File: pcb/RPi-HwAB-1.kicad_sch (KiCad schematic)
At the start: 8 parts, among them J1 GPIO, J2 Hirose_FH12-16S, J3 TC2050, U1 CAT24C256

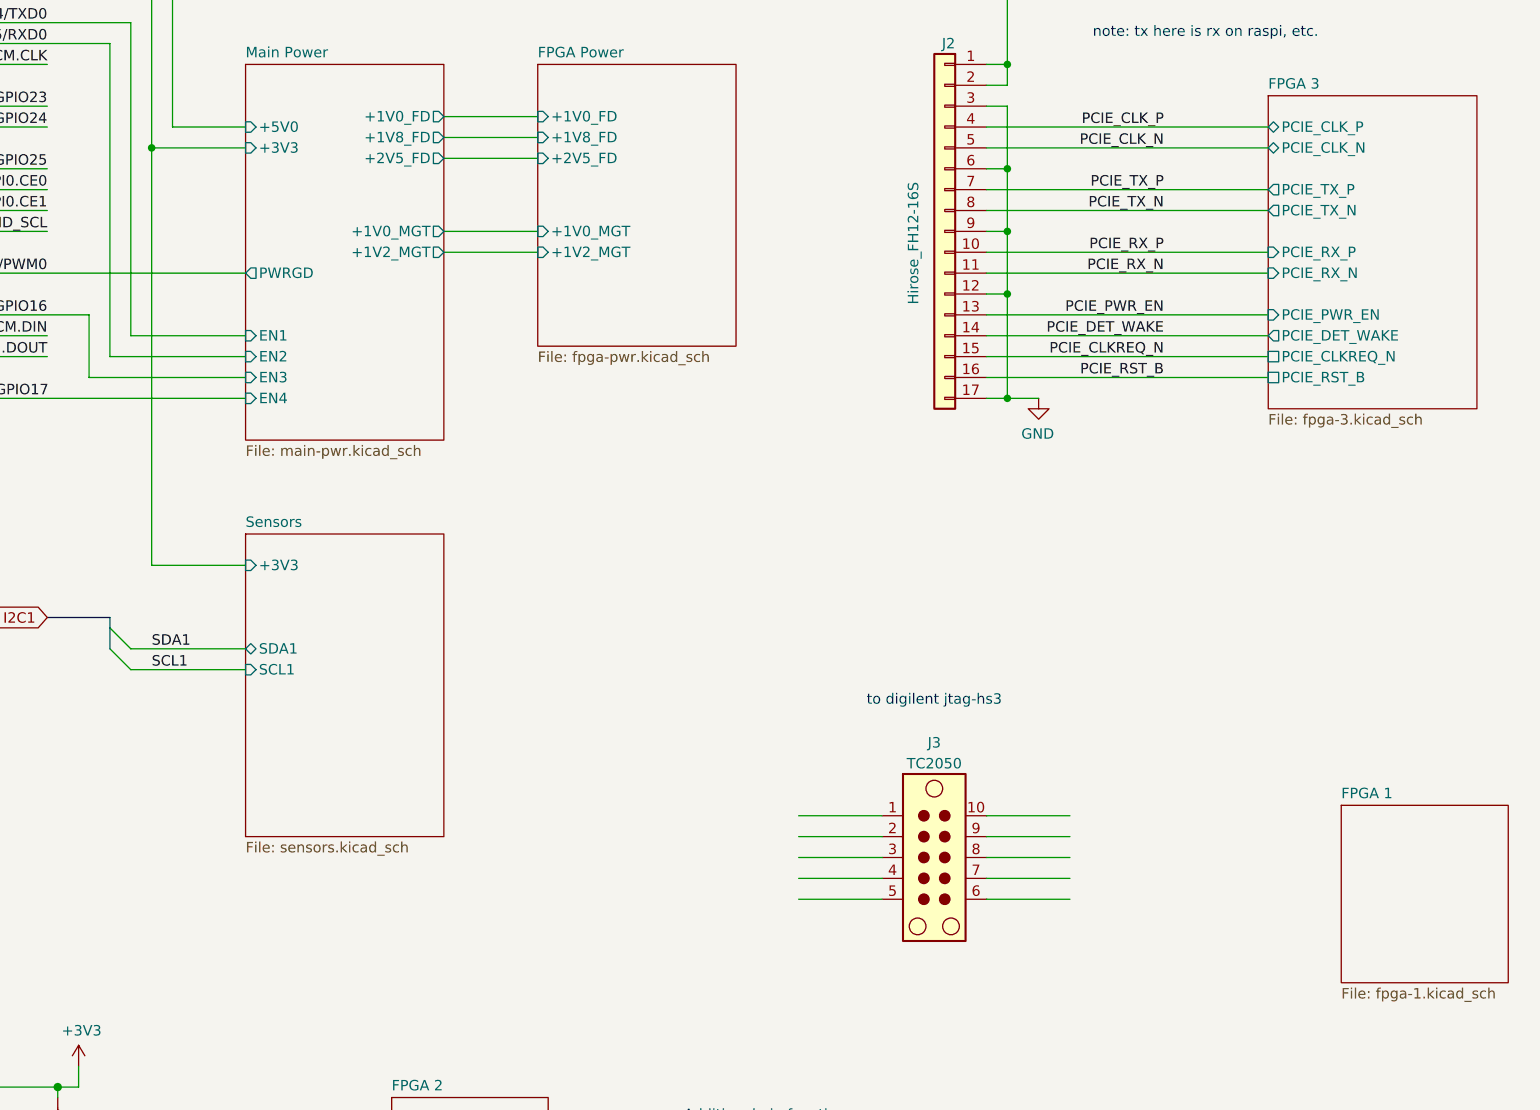
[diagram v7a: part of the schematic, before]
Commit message: connected jtag-fpga, tc2030
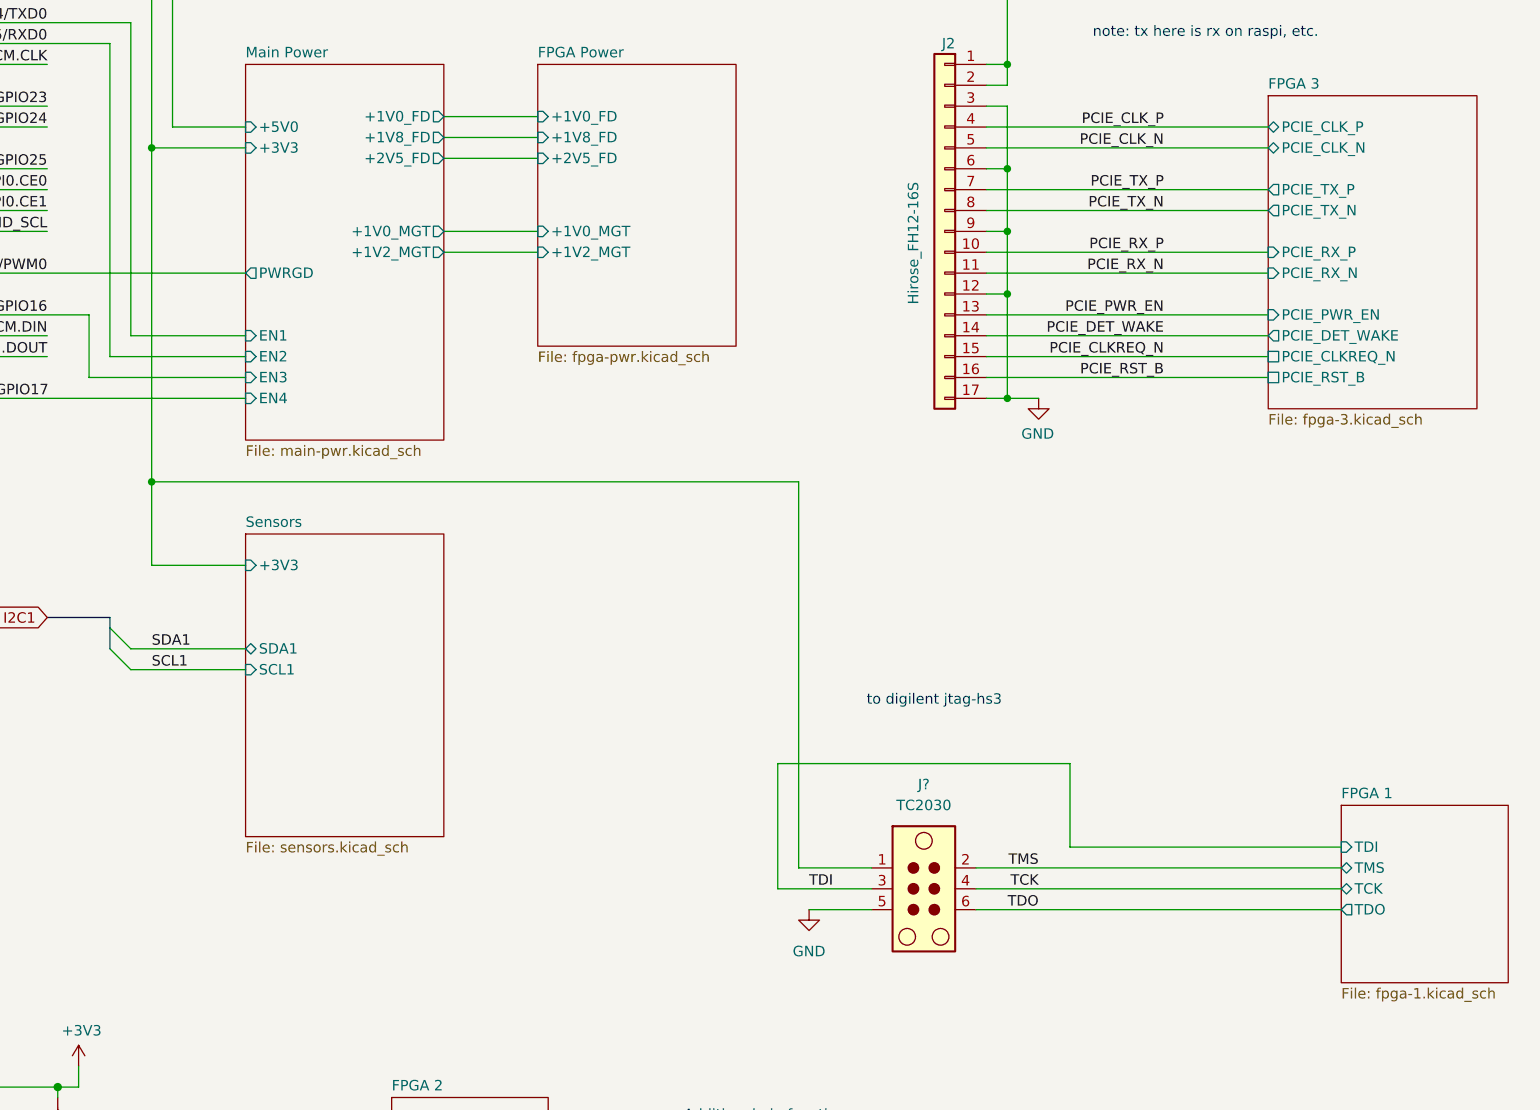
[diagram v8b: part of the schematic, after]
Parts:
- removed J3: TC2050, Connector:Tag-Connect_TC2050-IDC-NL_2x05_P1.27mm_Vertical, symbol Connector:TC2050
- added J?: TC2030, Connector:Tag-Connect_TC2030-IDC-NL_2x03_P1.27mm_Vertical, symbol Connector:TC2030
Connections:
- net +3V3: now also J?.1
- net GND: now also J?.5
- new net TCK: J?.4
- new net TDI: J?.3
- new net TDO: J?.6
- new net TMS: J?.2
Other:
- sheet FPGA 1 ports: added TCK, TDI, TDO, TMS; removed none
